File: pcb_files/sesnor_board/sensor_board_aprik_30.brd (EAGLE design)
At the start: 7 parts

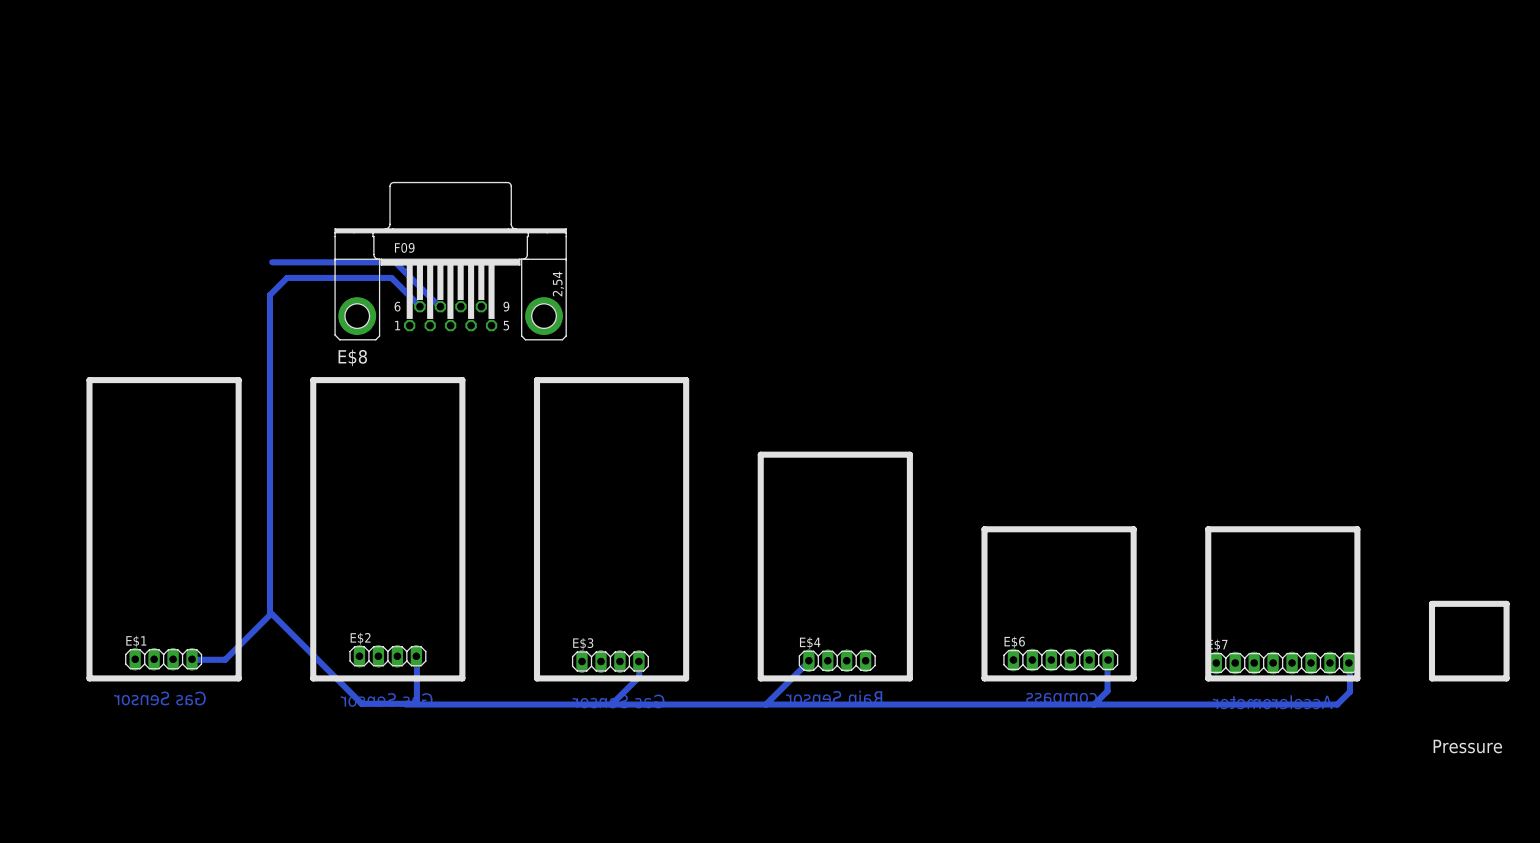
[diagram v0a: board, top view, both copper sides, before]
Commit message: Update to sensor board
Board now contains, 3x gas sensor, 1 compass, 1 pressure sensor, 1 rain
sensor, 1 accelerometer.
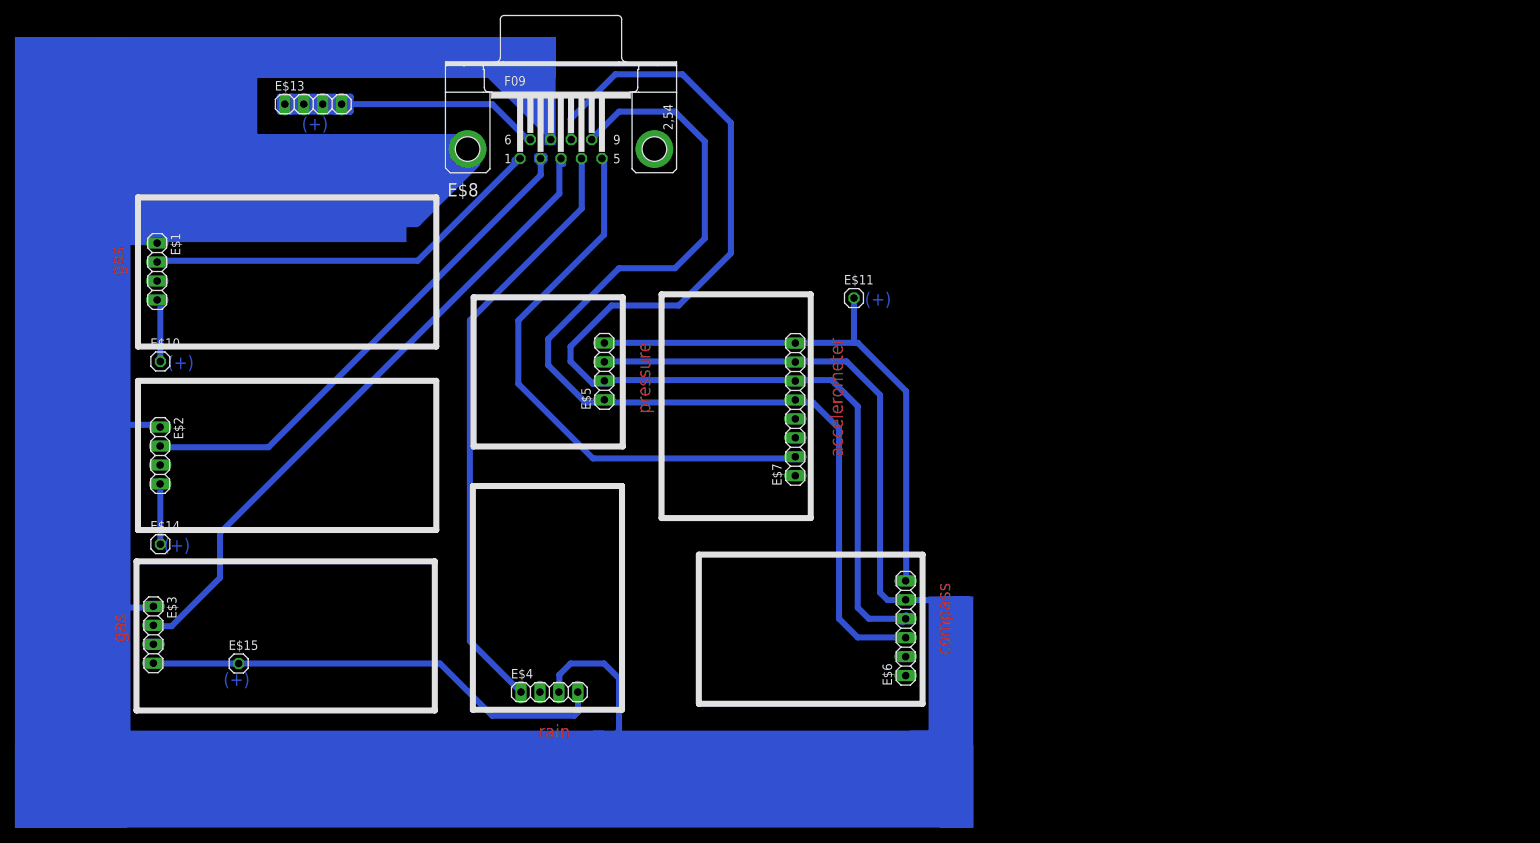
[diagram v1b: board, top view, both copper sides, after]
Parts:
- added E$10, E$11, E$14, E$15: (no value), pinhead:1X01
- added E$13, E$5: (no value), pinhead:1X04
- moved E$7 73.7 mm to (104.6, 56.1), turned to 90 degrees
- moved E$3 61.4 mm to (18.6, 25.9), turned to 270 degrees
- moved E$1 52.0 mm to (19.1, 74.6), turned to 270 degrees
- moved E$2 40.7 mm to (19.5, 49.9), turned to 270 degrees
- moved E$4 38.8 mm to (71.7, 18.2)
- moved E$8 26.8 mm to (73.2, 91.0)
- moved E$6 21.2 mm to (119.4, 26.7), turned to 90 degrees
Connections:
- new net S$3: E$10.1
- new net S$4: E$14.1
- new net S$6: E$15.1
- new net S$9: E$11.1
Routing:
- net S$13: track 0.00 -> 373.5 mm
- net S$3: track 154.5 -> 9.00 mm
- net S$18: track 0.00 -> 140.5 mm
- net S$17: track 0.00 -> 87.7 mm
- net S$19: track 0.00 -> 82.1 mm
- net S$16: track 0.00 -> 81.1 mm
- net S$21: track 0.00 -> 77.6 mm
- net S$9: track 0.00 -> 76.2 mm
- net S$22: track 0.00 -> 69.8 mm
- net S$20: track 0.00 -> 69.8 mm
- net S$7: track 0.00 -> 68.6 mm
- net S$6: track 0.00 -> 64.1 mm
- net S$5: track 0.00 -> 55.3 mm
- net S$1: track 78.8 -> 34.1 mm
- net S$4: track 25.1 -> 8.50 mm
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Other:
- board text added: "(+)"
- board text added: "(-)"
- board text added: "accelerometer"
- board text added: "gas"
- board text added: "pressure"
- board text added: "rain"
- board text removed: "Accelerometer"
- board text removed: "Gas Sensor"
- board text removed: "Pressure"
- board text removed: "Rain Sensor"
